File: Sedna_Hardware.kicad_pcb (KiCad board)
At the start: 2 copper layers, 43 parts, among them J1 PJ-102A, J10 Conn_01x02, J11 Conn_01x03, J2 Conn_02x05_Odd_Even, J3 0878340619, J4 Screw_Terminal_01x02, J5 Screw_Terminal_01x02, J6 Conn_01x14, J7 Conn_01x03, J8 Conn_01x03, J9 Conn_01x03, K1 ALDP105W, K2 ALDP105W, Q1 2N7000-D75Z, Q2 2N7000-D75Z, U1 LD1117V33, U2 ESP32-WROOM-32E, U3 LM6511IMX/NOPB

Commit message: Untangled rat net
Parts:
- removed the C3 at (66.0, 142.2)
- added C13: 1uF, Capacitor_THT:C_Disc_D9.0mm_W5.0mm_P5.00mm, F.Cu at (131.1, 116.3)
- added C4: 10uF, Capacitor_THT:C_Disc_D9.0mm_W5.0mm_P5.00mm, F.Cu at (150.4, 102.1)
- added R7: 110, Resistor_THT:R_Axial_DIN0204_L3.6mm_D1.6mm_P5.08mm_Horizontal, F.Cu at (138.7, 117.8)
- added R8: 10k, Resistor_THT:R_Axial_DIN0204_L3.6mm_D1.6mm_P5.08mm_Horizontal, F.Cu at (134.6, 113.2)
- R1: renamed from R2; value 10k -> 100k
- R3: renamed from R4; value 10k -> 100k
- U1: footprint digikey-footprints:TO-220-3 -> Package_TO_SOT_THT:TO-220-3_Horizontal_TabDown
- U2: value ESP32-WROOM-32E -> ESP32-WROOM-32D-N16; footprint Espressif:ESP32-WROOM-32E -> RF_Module:ESP32-WROOM-32
- moved C9 137.4 mm to (170.7, 76.7), turned to -90 degrees
- moved C5 128.5 mm to (177.8, 104.6), turned to 180 degrees
- moved C7 106.3 mm to (126.0, 65.5)
- moved C6 103.0 mm to (143.3, 116.8), turned to 90 degrees
- moved C8 102.1 mm to (138.2, 98.0)
- moved C12 81.8 mm to (120.4, 118.3), turned to 90 degrees
- moved RV1 71.3 mm to (120.4, 103.6), turned to 90 degrees
- moved J7 64.5 mm to (163.3, 76.7)
- moved C14 63.3 mm to (127.0, 98.0)
- moved R9 62.4 mm to (124.5, 108.7), turned to 90 degrees
- moved R6 59.5 mm to (150.9, 118.4), turned to 90 degrees
- moved J5 56.2 mm to (139.2, 92.7), turned to 90 degrees
- moved J8 43.2 mm to (120.4, 65.5)
- moved R10 33.0 mm to (132.1, 93.9), turned to 180 degrees
- moved J4 29.1 mm to (150.6, 121.6)
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- renumbered C12 to C10, C13 to C11, C10 to C12, C9 to C14, C5 to C2, C2 to C3, C6 to C5, C11 to C6, C4 to C9, D2 to D1, D3 to D2, D1 to D3, J11 to J10, J7 to J11, J4 to J2, J5 to J3, J10 to J4, J2 to J5, J8 to J6, J3 to J7, J6 to J8, R7 to R10, R3 to R2, R5 to R4, R1 to R5, R8 to R6, R6 to R9
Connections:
- D1 pad 1: Net-(D2-Pad1) -> +5V
- D1 pad 2: +5V -> Net-(D1-Pad2)
- D2 pad 1: Net-(K2-Pad1) -> +5V
- D2 pad 2: +5V -> Net-(D2-Pad2)
- J11 pad 2: Net-(J7-Pad2) -> Net-(J11-Pad2)
- J11 pad 3: Net-(C8-Pad1) -> +3V3
- J6 pad 2: TEMP_SEN -> Net-(J6-Pad2)
- J7 pad 4: +3V3 -> unconnected-(J7-Pad4)
- K1 pad 1: Net-(D2-Pad1) -> Net-(D1-Pad2)
- K2 pad 1: Net-(K2-Pad1) -> Net-(D2-Pad2)
- Q1 pad 3: Net-(D2-Pad1) -> Net-(D1-Pad2)
- Q2 pad 3: Net-(K2-Pad1) -> Net-(D2-Pad2)
- U2 pad 39: (no net) -> GND
- U2 pad 4: TOUCH_CS -> LCD_BRIGHTNESS
- U2 pad 7: LCD_BRIGHTNESS -> TOUCH_CS
- U2 pad 8: unconnected-(U2-Pad8) -> LCD_RESET
- U3 pad 3: Net-(J7-Pad2) -> Net-(R8-Pad1)

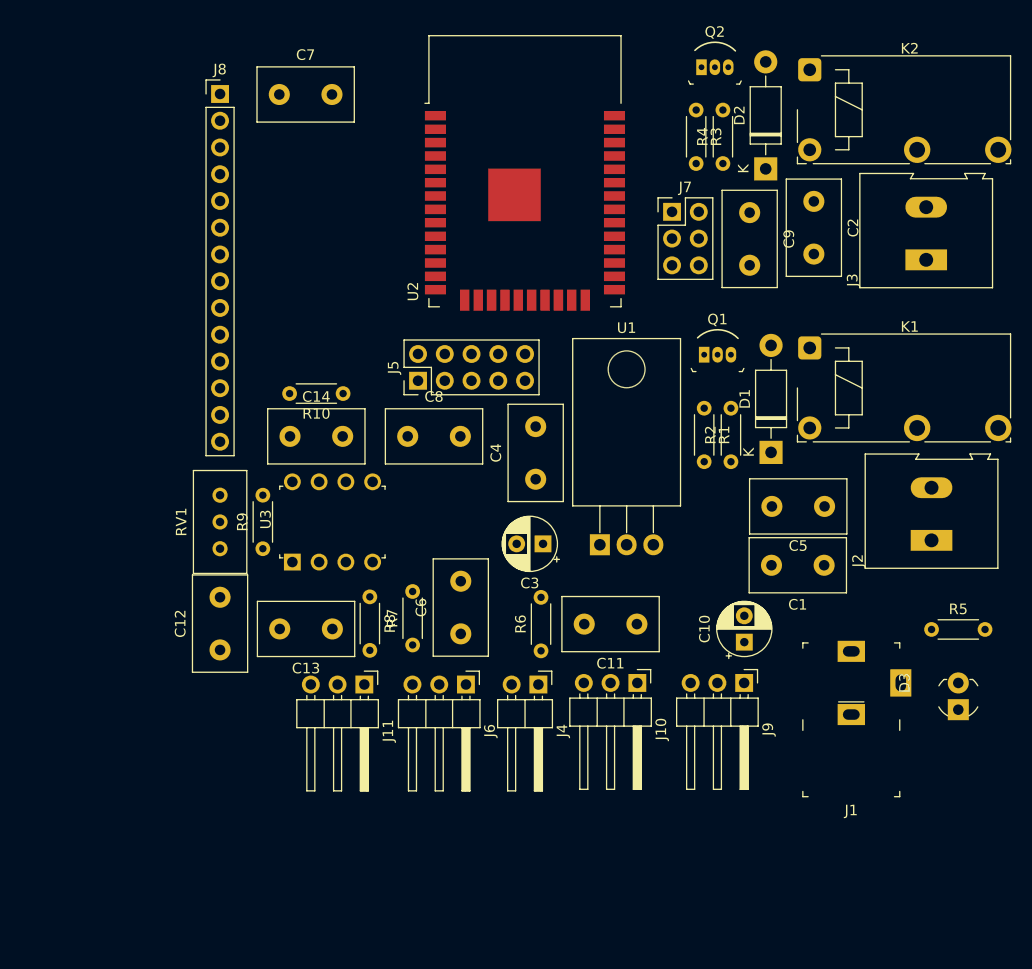
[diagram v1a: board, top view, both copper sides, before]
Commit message: Fixed schematic and pcb placement. added mounting holes
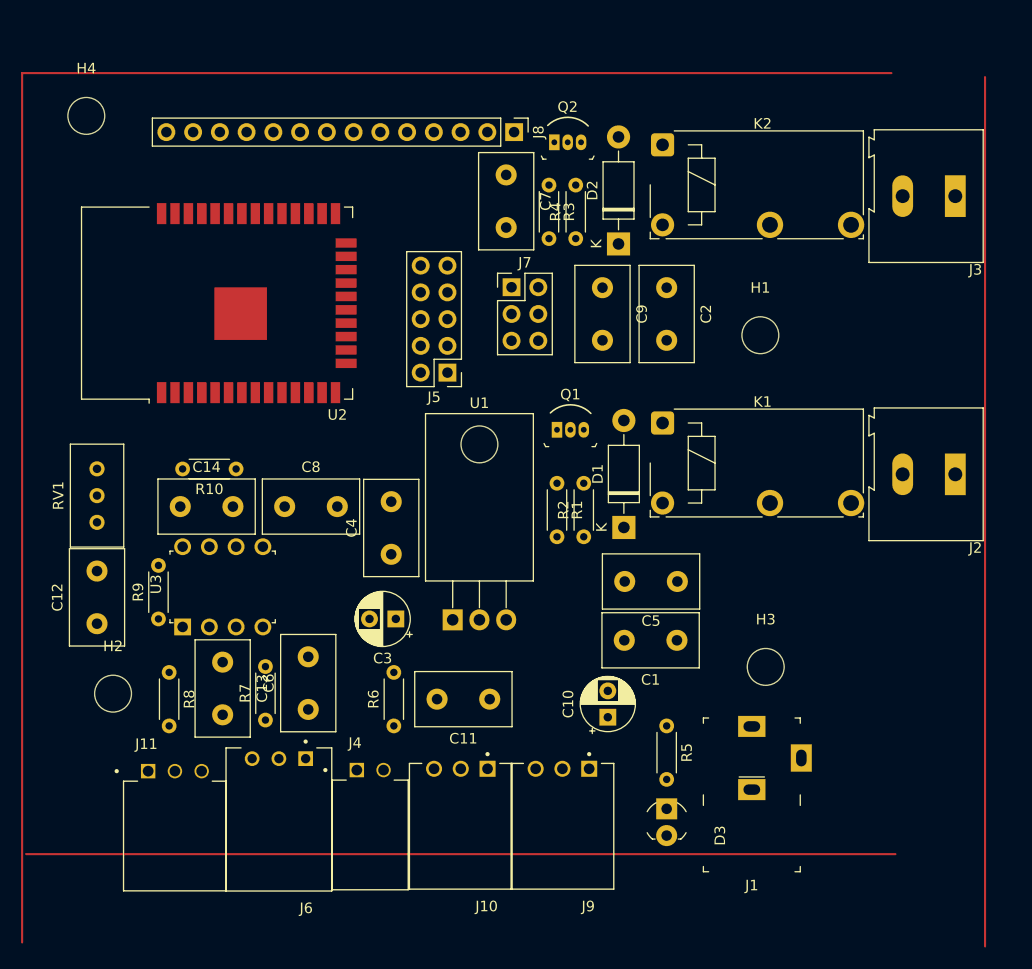
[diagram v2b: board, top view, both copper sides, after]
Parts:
- added H1: Mounting_Hole, MountingHole:MountingHole_3.5mm, F.Cu at (171.7, 88.4)
- added H2: Mounting_Hole, MountingHole:MountingHole_3.5mm, F.Cu at (110.2, 122.4)
- added H3: Mounting_Hole, MountingHole:MountingHole_3.5mm, F.Cu at (172.2, 119.9)
- added H4: Mounting_Hole, MountingHole:MountingHole_3.5mm, F.Cu at (107.7, 67.6)
- J10, J9: value Conn_01x03 -> 2-644803-3; footprint Connector_PinHeader_2.54mm:PinHeader_1x03_P2.54mm_Horizontal -> 2-644803-3:TE_2-644803-3
- J11: value Conn_01x03 -> 2-644488-3; footprint Connector_PinHeader_2.54mm:PinHeader_1x03_P2.54mm_Horizontal -> 2-644488-3:TE_2-644488-3
- J4: value Conn_01x02 -> 2-644488-2; footprint Connector_PinHeader_2.54mm:PinHeader_1x02_P2.54mm_Horizontal -> 2-644488-2:TE_2-644488-2
- J5: value Conn_02x05_Odd_Even -> 61201021721
- J6: value Conn_01x03 -> 5-103634-2; footprint Connector_PinHeader_2.54mm:PinHeader_1x03_P2.54mm_Horizontal -> 5-103634-2:TE_5-103634-2
- moved D3 31.3 mm to (162.8, 135.9), turned to -90 degrees
- moved J8 28.2 mm to (148.3, 69.1), turned to -90 degrees
- moved U2 27.9 mm to (123.1, 85.3), turned to 90 degrees
- moved R5 26.8 mm to (162.8, 125.5), turned to -90 degrees
- moved C7 22.9 mm to (147.6, 73.2), turned to -90 degrees
- moved J11 22.1 mm to (113.6, 129.8), turned to 0 degrees
- moved R8 20.4 mm to (115.6, 120.4)
- moved J6 19.1 mm to (126.0, 128.6), turned to 180 degrees
- moved J9 19.1 mm to (152.9, 129.6), turned to 180 degrees
- moved J4 19.1 mm to (133.4, 129.7), turned to 0 degrees
- moved J10 18.6 mm to (143.3, 129.6), turned to 180 degrees
- moved J7 16.8 mm to (148.1, 83.8)
- moved C2 16.2 mm to (162.8, 83.9)
- moved C6 16.2 mm to (128.8, 123.9)
- moved K2 15.7 mm to (162.4, 70.3)
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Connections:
- J4 pad 1: FLOAT_SEN_INT -> FLOAT_SEN_IN
- J7 pad 4: unconnected-(J7-Pad4) -> GND
- J8 pad 8: LCD_BRIGHTNESS -> unconnected-(J8-Pad8)
- R10 pad 1: LIQUID_SEN_INT -> LIQUID_SEN_IN
- R6 pad 1: FLOAT_SEN_INT -> FLOAT_SEN_IN
- R7 pad 2: TEMP_SEN -> TEMP_SEN_IN
- U2 pad 10: LIQUID_SEN_INT -> TOUCH_IRQ
- U2 pad 27: TEMP_SEN -> TOUCH_CS
- U2 pad 29: FLOAT_SEN_INT -> LCD_DC/RS
- U2 pad 4: LCD_BRIGHTNESS -> TEMP_SEN_IN
- U2 pad 5: TOUCH_IRQ -> unconnected-(U2-Pad5)
- U2 pad 6: LCD_DC/RS -> LIQUID_SEN_IN
- U2 pad 7: TOUCH_CS -> FLOAT_SEN_IN
- U3 pad 3: Net-(R8-Pad1) -> Net-(R8-Pad2)
- U3 pad 7: LIQUID_SEN_INT -> LIQUID_SEN_IN

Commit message: based PCB layout
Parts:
- U3: footprint digikey-footprints:DIP-8_W7.62mm -> Package_SO:SOIC-8_3.9x4.9mm_P1.27mm
- moved C9 45.6 mm to (180.8, 45.2)
- moved J7 42.4 mm to (166.6, 45.7)
- moved H1 26.4 mm to (188.0, 67.6)
- moved J8 25.2 mm to (173.5, 67.1)
- moved C7 18.3 mm to (149.4, 91.4), turned to 90 degrees
- moved H3 16.0 mm to (188.0, 122.9)
- moved H4 15.7 mm to (123.4, 67.6)
- moved C2 13.3 mm to (168.1, 96.0), turned to 180 degrees
- moved J3 12.4 mm to (192.5, 87.4)
- moved K2 12.4 mm to (164.7, 82.5)
- moved D2 11.6 mm to (161.3, 91.0)
- moved Q2 11.6 mm to (155.2, 81.3)
- moved R3 10.9 mm to (153.9, 84.8)
- moved R4 10.9 mm to (156.5, 89.9)
- moved C5 7.14 mm to (163.1, 118.9), turned to 0 degrees
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
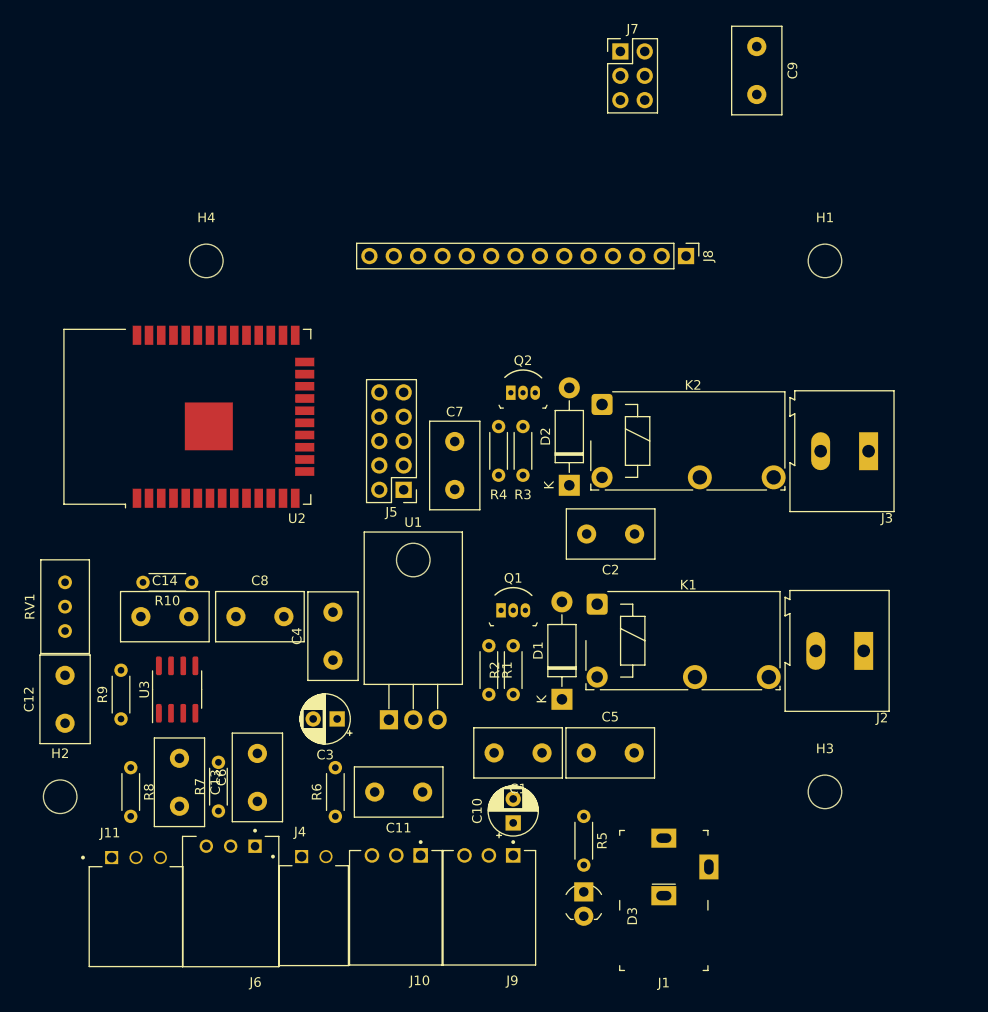
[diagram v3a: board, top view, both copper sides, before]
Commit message: started layout tracks. Fixed regulator footprint
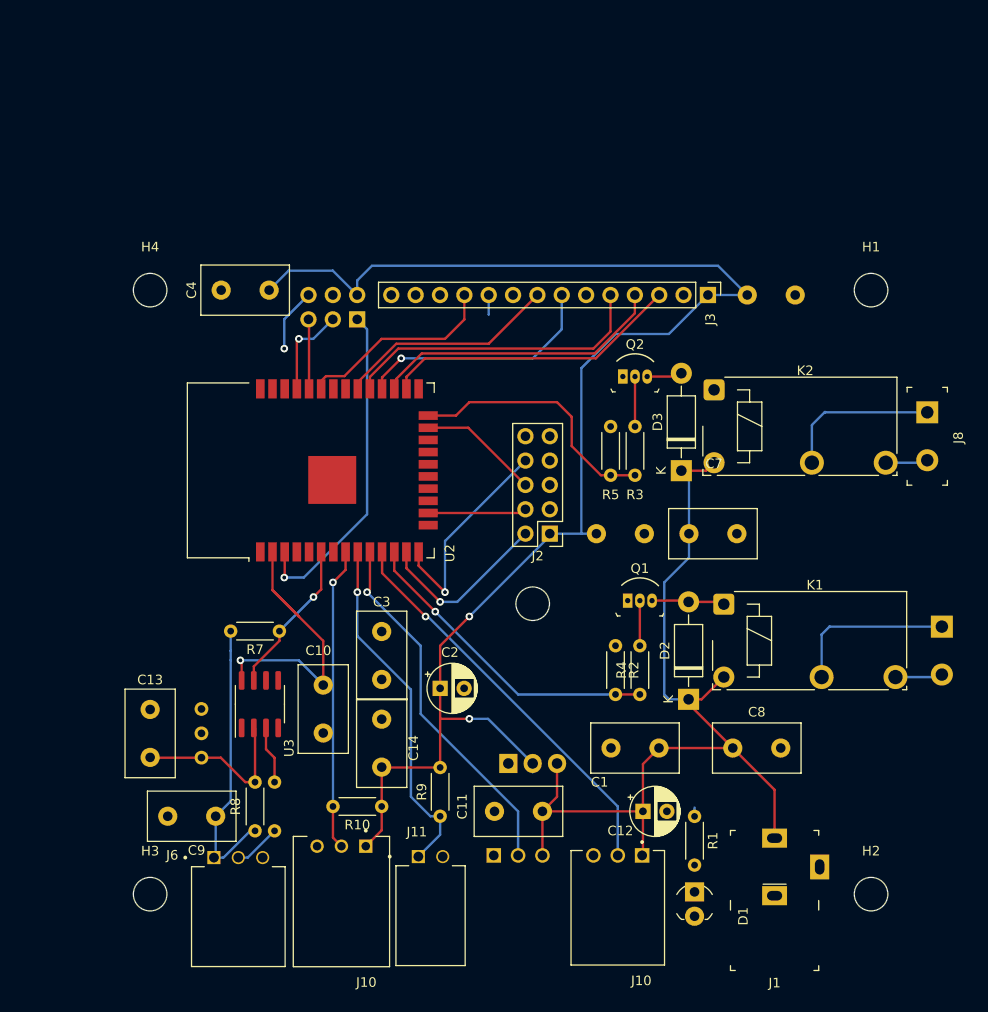
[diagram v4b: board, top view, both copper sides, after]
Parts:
- removed the C8 at (126.5, 104.7)
- removed the J10 at (143.3, 129.6)
- removed the J11 at (113.6, 129.8)
- removed the J2 at (192.0, 108.2)
- removed the J3 at (192.5, 87.4)
- removed the R7 at (124.7, 124.9)
- removed the R8 at (115.6, 120.4)
- added C5: 1uF, Capacitor_THT:C_Disc_D9.0mm_W5.0mm_P5.00mm, B.Cu at (164.1, 96.0)
- added J5: 2-644803-3, 2-644803-3:TE_2-644803-3, B.Cu at (156.0, 129.6)
- added J6: 2-644488-3, 2-644488-3:TE_2-644488-3, F.Cu at (124.2, 129.8)
- added J7: 1935161, digikey-footprints:Terminal_Block_D1.3mm_P5mm, B.Cu at (200.2, 105.7)
- added J8: 1935161, digikey-footprints:Terminal_Block_D1.3mm_P5mm, F.Cu at (198.6, 83.4)
- added R10: 110, Resistor_THT:R_Axial_DIN0204_L3.6mm_D1.6mm_P5.08mm_Horizontal, F.Cu at (141.7, 124.5)
- added R6: 10k, Resistor_THT:R_Axial_DIN0204_L3.6mm_D1.6mm_P5.08mm_Horizontal, B.Cu at (130.6, 127.0)
- C6: renamed from C9; moved to B.Cu
- J4: renamed from J7; moved to B.Cu
- RV1: moved to B.Cu
- U1: footprint Package_TO_SOT_THT:TO-220-3_Horizontal_TabDown -> Package_TO_SOT_THT:TO-220-3_Horizontal_TabUp; moved to B.Cu
- moved J4 39.2 mm to (139.2, 73.7), turned to 90 degrees
- moved C4 28.4 mm to (130.0, 70.6), turned to 180 degrees
- moved C6 25.9 mm to (179.9, 71.1), turned to 0 degrees
- moved C10 20.3 mm to (135.6, 111.8), turned to -90 degrees
- moved RV1 19.4 mm to (122.9, 114.3)
- moved J2 15.9 mm to (159.3, 96.0)
- moved R8 15.5 mm to (128.5, 121.9), turned to -90 degrees
- moved C8 15.3 mm to (178.3, 118.4)
- moved U2 14.0 mm to (137.3, 89.4)
- moved H3 13.8 mm to (117.6, 133.6)
- moved C12 13.6 mm to (169.0, 125.0), turned to 0 degrees
- moved J10 13.4 mm to (166.4, 129.6)
- moved C14 13.4 mm to (141.7, 120.4)
- moved U1 13.3 mm to (154.9, 120.0)
- moved Q1 13.2 mm to (167.4, 103.0)
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- renumbered C14 to C10, C10 to C12, C12 to C13, C6 to C14, C3 to C2, C4 to C3, C7 to C4, C2 to C7, C5 to C8, C13 to C9, D3 to D1, D1 to D2, D2 to D3, H3 to H2, H2 to H3, J6 to J10, J9 to J10, J4 to J11, J5 to J2, J8 to J3, R5 to R1, R1 to R2, R2 to R4, R4 to R5, R10 to R7, R9 to R8, R6 to R9
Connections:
- J10 pad 2: Net-(J6-Pad2) -> TEMP_SEN_IN
- J3 pad 8: unconnected-(J8-Pad8) -> LCD_Brightness
- U2 pad 10: TOUCH_IRQ -> LED_STRIP_CTRL
- U2 pad 11: LED_STRIP_CTRL -> SERVO_CTRL
- U2 pad 12: SERVO_CTRL -> RELAY_CTRL_1
- U2 pad 24: RELAY_CTRL_1 -> RELAY_CTRL_2
- U2 pad 26: RELAY_CTRL_2 -> LCD_CS
- U2 pad 27: TOUCH_CS -> LCD_RESET
- U2 pad 30: LCD_TOUCH_CLK -> LCD_Brightness
- U2 pad 33: MOSI_LCD -> TOUCH_CS
- U2 pad 36: MISO_LCD -> TOUCH_IRQ
- U2 pad 4: TEMP_SEN_IN -> unconnected-(U2-Pad4)
- U2 pad 7: FLOAT_SEN_IN -> unconnected-(U2-Pad7)
- U2 pad 8: LCD_RESET -> TEMP_SEN_IN
- U2 pad 9: LCD_CS -> FLOAT_SEN_IN
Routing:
- net +3V3: track 0.00 -> 217.0 mm, vias 0 -> 3
- net +5V: track 0.00 -> 94.4 mm
- net SERVO_CTRL: track 0.00 -> 42.1 mm, vias 0 -> 1
- net LED_STRIP_CTRL: track 0.00 -> 38.3 mm, vias 0 -> 1
- net FLOAT_SEN_IN: track 0.00 -> 36.9 mm, vias 0 -> 1
- net PROG_EN: track 0.00 -> 34.8 mm, vias 0 -> 1
- net RELAY_CTRL_1: track 0.00 -> 32.9 mm, vias 0 -> 1
- net LCD_DC/RS: track 0.00 -> 32.1 mm
- net TEMP_SEN_IN: track 0.00 -> 31.6 mm, vias 0 -> 1
- net LCD_CS: track 0.00 -> 31.1 mm
- net LCD_RESET: track 0.00 -> 30.7 mm
- net LCD_TOUCH_CLK: track 0.00 -> 27.6 mm, vias 0 -> 1
- net RELAY_CTRL_2: track 0.00 -> 27.1 mm
- net LCD_Brightness: track 0.00 -> 23.2 mm
- net JTAG_TDI: track 0.00 -> 22.5 mm, vias 0 -> 1
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
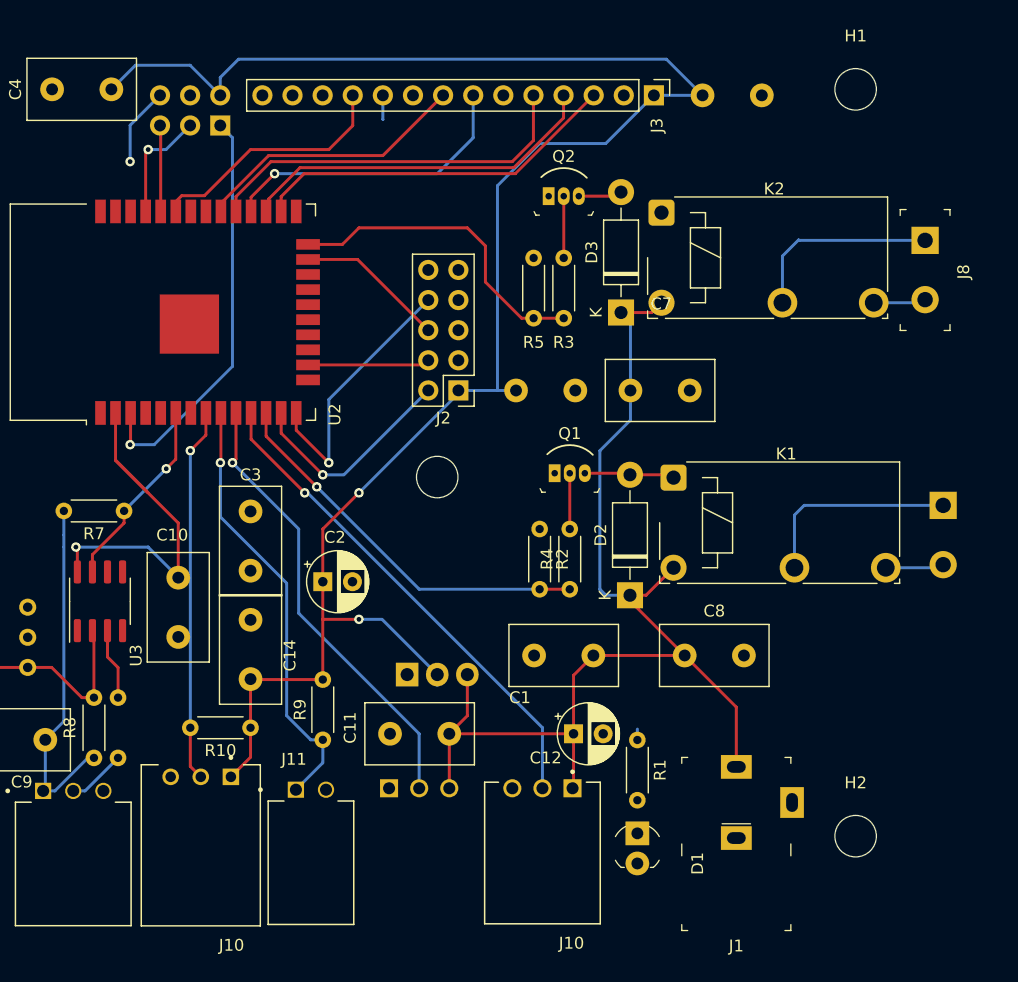
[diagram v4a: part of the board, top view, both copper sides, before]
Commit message: adjusted track size of power bus
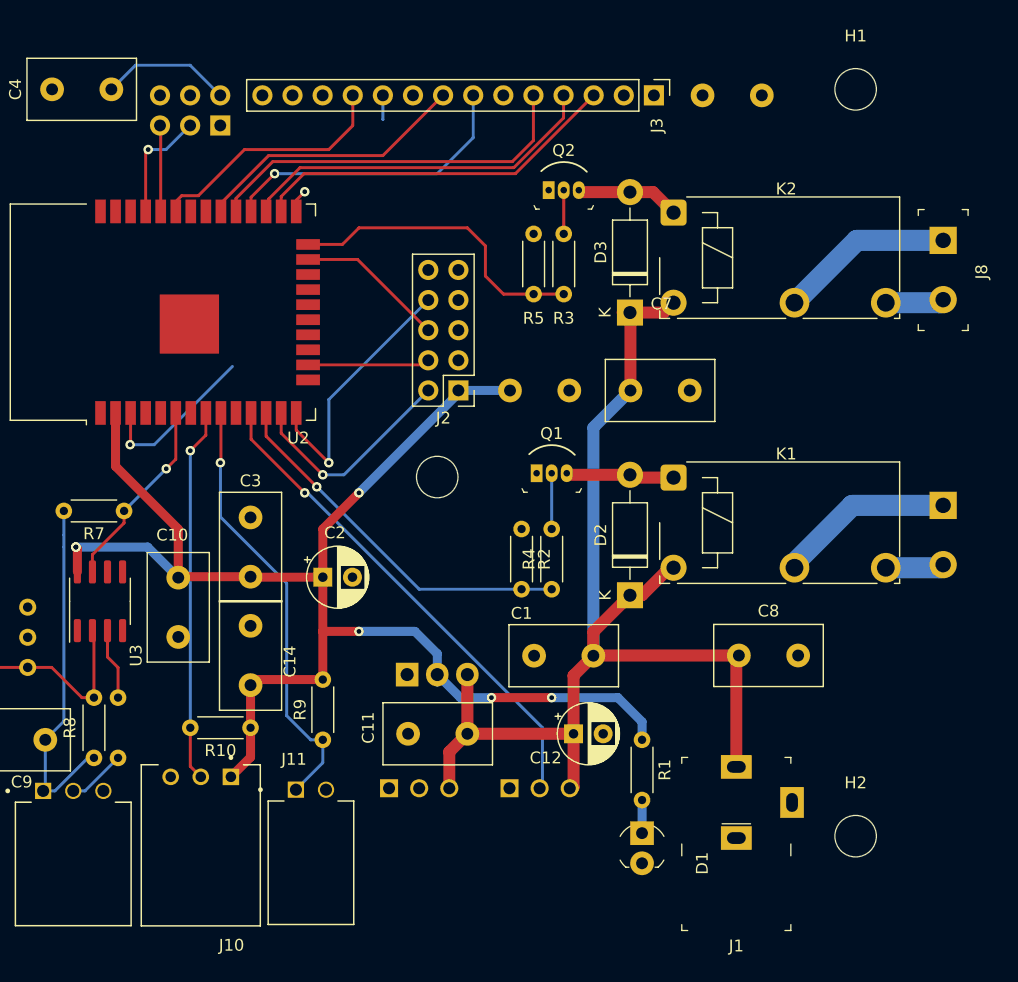
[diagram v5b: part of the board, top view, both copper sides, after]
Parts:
- removed the J10 at (166.4, 129.6)
- added J9: 2-644803-3, 2-644803-3:TE_2-644803-3, B.Cu at (166.1, 129.6)
- moved C8 4.57 mm to (182.9, 118.4)
- moved R3 2.03 mm to (165.6, 82.8)
- moved R5 2.03 mm to (168.1, 87.9)
- moved C11 1.52 mm to (160.0, 125.0)
- moved J8 1.52 mm to (200.2, 83.4)
- moved Q1 1.52 mm to (165.9, 103.0)
- moved R2 1.52 mm to (164.6, 107.7)
- moved R4 1.52 mm to (167.1, 112.8)
- moved K2 1.02 mm to (177.4, 81.0)
- moved D3 0.76 mm to (173.7, 89.4)
- moved C14 0.51 mm to (141.7, 120.9)
- moved Q2 0.51 mm to (166.9, 79.1)
- moved C3 0.51 mm to (141.7, 111.7)
- moved C5 0.51 mm to (163.6, 96.0)
- moved D1 0.39 mm to (174.8, 135.9)
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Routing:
- net +3V3: track 217.0 -> 162.3 mm, vias 3 -> 6
- net LED_STRIP_CTRL: track 38.3 -> 0.00 mm, vias 1 -> 0
- net PROG_EN: track 34.8 -> 14.1 mm
- net +5V: track 94.4 -> 100.1 mm
- net Net-(D3-Pad2): track 3.71 -> 8.78 mm
- net PROG_IO0: track 6.63 -> 1.96 mm
- net Net-(D1-Pad1): track 0.00 -> 2.79 mm
- net Net-(J7-Pad1): track 17.3 -> 15.1 mm
- net Net-(D2-Pad2): track 7.64 -> 9.82 mm
- net Net-(J8-Pad1): track 16.5 -> 14.7 mm
- net RELAY_CTRL_1: track 32.9 -> 31.4 mm
- net Net-(Q2-Pad2): track 5.21 -> 3.69 mm
- net RELAY_CTRL_2: track 27.1 -> 25.9 mm
- net Net-(J8-Pad2): track 4.44 -> 4.95 mm
